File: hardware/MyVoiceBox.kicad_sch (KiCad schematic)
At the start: 22 parts, among them J1 USB_B_Micro, J2 Gain Select, J3 AudioJack3, SW1 BOOT, SW2 RESET, U2 HT7833, U3 INMP441, U4 INMP441, U6 Debug Serial Port

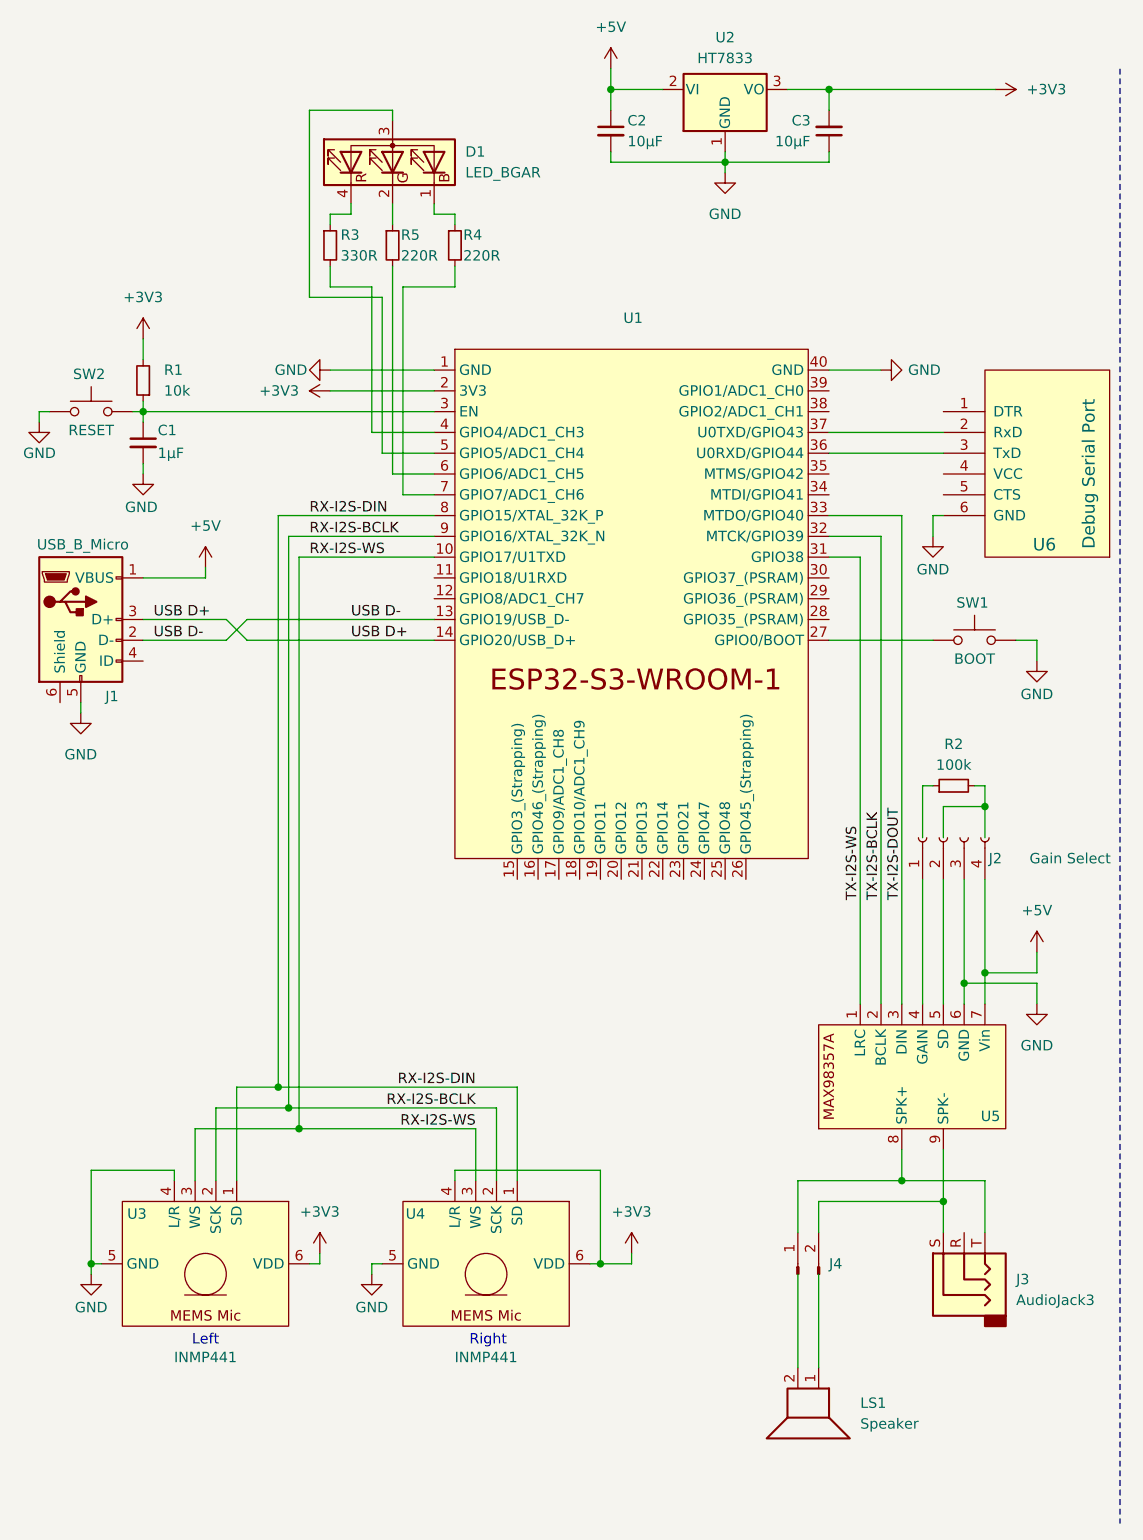
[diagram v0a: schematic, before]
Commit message: sioem cleanup, updated README, updated schematic
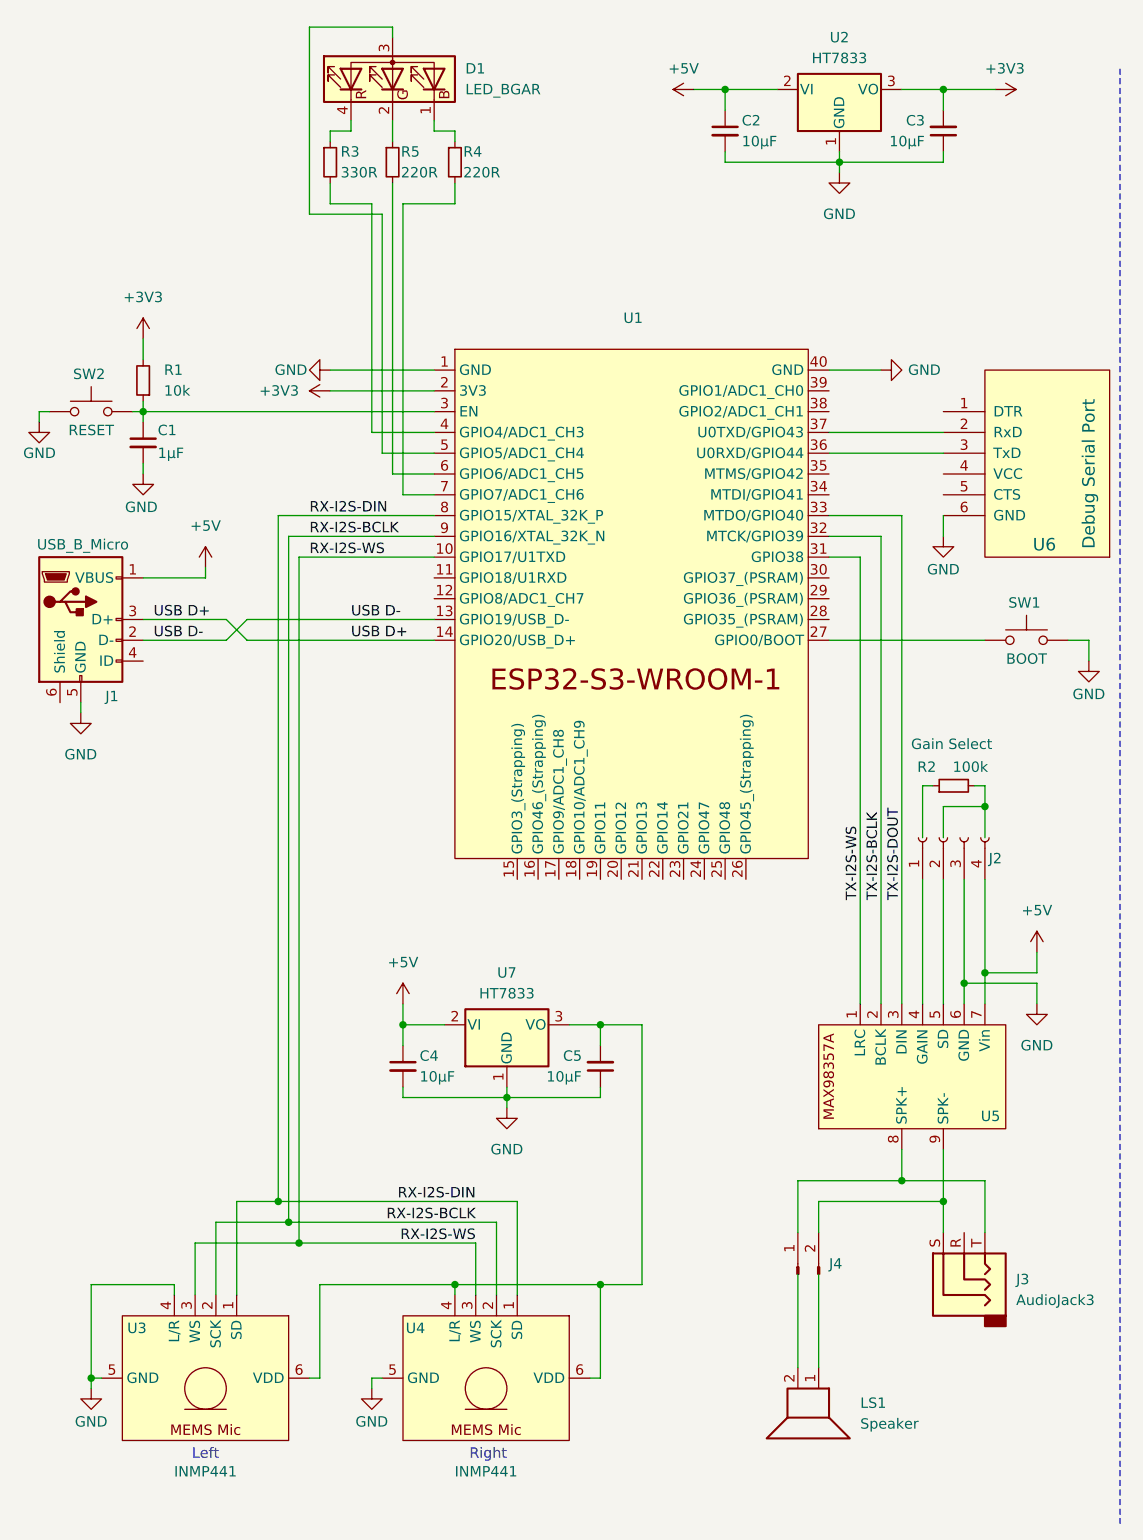
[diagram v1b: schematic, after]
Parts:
- added C4, C5: 10µF, symbol Device:C_Small
- added U7: HT7833, Package_TO_SOT_THT:TO-92_Inline, symbol Regulator_Linear:MCP1700x-500xxTO
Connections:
- net +3V3: no longer U3.6 (VDD), U4.4 (L/R), U4.6 (VDD)
- net +5V: now also C4.1, U7.2 (VI)
- net GND: now also C4.2, C5.1, U7.1 (GND)
- new net: C5.2, U3.6 (VDD), U4.4 (L/R), U4.6 (VDD), U7.3 (VO)
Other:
- moved on the sheet: C2, C3, D1, R3, R4, R5, SW1, U2, U3, U4
